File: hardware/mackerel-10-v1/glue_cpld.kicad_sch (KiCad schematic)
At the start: 19 parts, among them J1 Conn_02x05_Odd_Even, J7 Conn_02x03_Odd_Even, X1 50MHz, X2 50MHz

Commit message: Mack-10 v1 fully routed
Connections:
- net /DTACK_EXP: now also U2.30 (IO); no longer U2.31 (IO)
- net /EXP: now also U2.28 (IO); no longer U2.29 (IO)
- net /IACK_EXP: now also U2.31 (IO); no longer U2.30 (IO)
- net /IRQ_EXP: now also U2.29 (IO); no longer U2.28 (IO)
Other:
- note removed: "SPI and I2C expansion"
- note removed: "TODO: GPIO with leftover pins"
- note removed: "TODO: SPI and I2C headers TODO: enough room on CPLD for this logic?"
- note removed: "TODO: control lines for IDE, DRAM, and expansion"
- note removed: "TODO: how many address pins are actually needed for decoding?"
- note removed: "TODO: probably don't need A4 - just A1-3 for IACK decode"
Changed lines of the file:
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@@
-		)
-	)
-	(text "TODO: how many address pins are actually needed for decoding?"
-		(exclude_from_sim no)
-		(at 66.802 97.282 0)
-		(effects
-			(font
-				(size 1.27 1.27)
-			)
-		)
-	)
-	(text "SPI and I2C expansion"
-		(exclude_from_sim no)
-		(at 227.076 159.004 0)
-		(effects
-			(font
-				(size 1.27 1.27)
-			)
-		)
-	)
-	(text "TODO: SPI and I2C headers\nTODO: enough room on CPLD for this logic?"
-		(exclude_from_sim no)
-		(at 221.488 102.108 0)
-		(effects
-			(font
-				(size 1.27 1.27)
-			)
-		)
-	)
-	(text "TODO: probably don't need A4 - just A1-3 for IACK decode"
-		(exclude_from_sim no)
-		(at 65.786 107.188 0)
-		(effects
-			(font
-				(size 1.27 1.27)
-			)
-		)
-	)
-	(text "TODO: GPIO with leftover pins"
-		(exclude_from_sim no)
-		(at 227.584 87.884 0)
-		(effects
-			(font
-				(size 1.27 1.27)
-			)
 		)
 	)
@@
 		)
 	)
-	(text "TODO: control lines for IDE, DRAM, and expansion"
-		(exclude_from_sim no)
-		(at 218.694 75.184 0)
-		(effects
-			(font
-				(size 1.27 1.27)
-			)
-		)
-	)
 	(global_label "CLK_ALT"
 		(shape input)
@@
 	(global_label "{slash}IRQ_EXP"
 		(shape input)
-		(at 113.03 130.81 180)
-		(fields_autoplaced yes)
-		(effects
-			(font
-				(size 1.27 1.27)
-			)
-			(justify right)
-		)
-		(property "Intersheetrefs" "${INTERSHEET_REFS}"
-			(at 100.9129 130.81 0)
+		(at 113.03 133.35 180)
+		(fields_autoplaced yes)
+		(effects
+			(font
+				(size 1.27 1.27)
+			)
+			(justify right)
+		)
+		(property "Intersheetrefs" "${INTERSHEET_REFS}"
+			(at 100.9129 133.35 0)
 			(effects
 				(font
@@
 	(global_label "{slash}IACK_EXP"
 		(shape output)
-		(at 113.03 135.89 180)
-		(fields_autoplaced yes)
-		(effects
-			(font
-				(size 1.27 1.27)
-			)
-			(justify right)
-		)
-		(property "Intersheetrefs" "${INTERSHEET_REFS}"
-			(at 99.8848 135.89 0)
+		(at 113.03 138.43 180)
+		(fields_autoplaced yes)
+		(effects
+			(font
+				(size 1.27 1.27)
+			)
+			(justify right)
+		)
+		(property "Intersheetrefs" "${INTERSHEET_REFS}"
+			(at 99.8848 138.43 0)
 			(effects
 				(font
@@
 	(global_label "{slash}EXP"
 		(shape output)
-		(at 113.03 133.35 180)
-		(fields_autoplaced yes)
-		(effects
-			(font
-				(size 1.27 1.27)
-			)
-			(justify right)
-		)
-		(property "Intersheetrefs" "${INTERSHEET_REFS}"
-			(at 105.0858 133.35 0)
+		(at 113.03 130.81 180)
+		(fields_autoplaced yes)
+		(effects
+			(font
+				(size 1.27 1.27)
+			)
+			(justify right)
+		)
+		(property "Intersheetrefs" "${INTERSHEET_REFS}"
+			(at 105.0858 130.81 0)
 			(effects
 				(font
@@
 	(global_label "{slash}DTACK_EXP"
 		(shape input)
-		(at 113.03 138.43 180)
-		(fields_autoplaced yes)
-		(effects
-			(font
-				(size 1.27 1.27)
-			)
-			(justify right)
-		)
-		(property "Intersheetrefs" "${INTERSHEET_REFS}"
-			(at 98.252 138.43 0)
-			(effects
-				(font
+		(at 113.03 135.89 180)
+		(fields_autoplaced yes)
+		(effects
+			(font
+				(size 1.27 1.27)
+			)
+			(justify right)
+		)
+		(property "Intersheetrefs" "${INTERSHEET_REFS}"
+			(at 98.252 135.89 0)
+			(effects
+				(font

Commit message: Mackerel-10 v1 release
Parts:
- added R24: R, Resistor_THT:R_Axial_DIN0207_L6.3mm_D2.5mm_P7.62mm_Horizontal, symbol Device:R
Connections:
- net +5V: now also R24.2
- net /IRQ_EXP: now also R24.1
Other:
- note removed: "TODO: user LED"
- moved on the sheet: C25, C26, C27, C28, C29, C30, C31, C32, C41, C42, X2

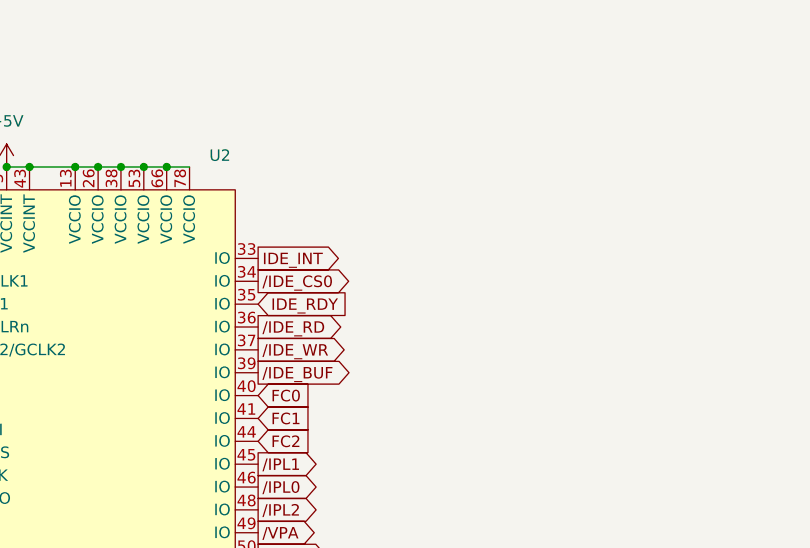
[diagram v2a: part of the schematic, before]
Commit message: Fix IDE buffer direction and add CS1 pin
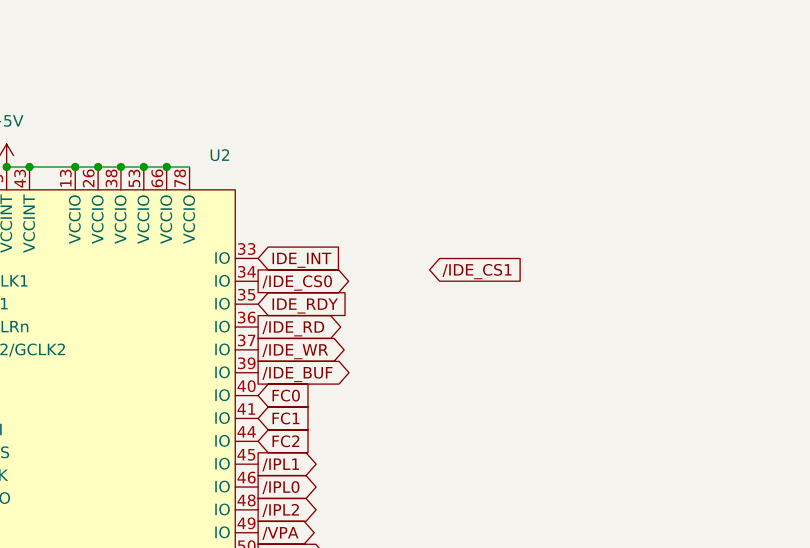
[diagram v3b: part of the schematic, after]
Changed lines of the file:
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@@
+		)
+	)
+	(global_label "{slash}IDE_CS1"
+		(shape input)
+		(at 166.37 49.53 0)
+		(fields_autoplaced yes)
+		(effects
+			(font
+				(size 1.27 1.27)
+			)
+			(justify left)
+		)
+		(property "Intersheetrefs" "${INTERSHEET_REFS}"
+			(at 178.3661 49.53 0)
+			(effects
+				(font
+					(size 1.27 1.27)
+				)
+				(justify left)
+				(hide yes)
+			)
 		)
 	)
@@
 	)
 	(global_label "IDE_INT"
-		(shape output)
+		(shape input)
 		(at 147.32 48.26 0)
 		(fields_autoplaced yes)
